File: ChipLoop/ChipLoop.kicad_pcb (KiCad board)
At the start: 2 copper layers, 100 x 60 mm, 33 parts, among them J1 Conn_02x25_Counter_Clockwise, J2 Jumper, Q1 2N3904, SW1 SW_A, SW2 SW_B, U1 ATtiny84A-PU, U2 ISD1820P, U3 L78L05_TO92

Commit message: Finalized changes to chip loop input and output
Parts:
- removed the C4 at (90.3, 85.0)
- removed the C5 at (176.2, 86.4)
- removed C6: 0.001uF, libraries:C_Flat_L7.2_H6.5
- added R1: 47K, Resistor_THT:R_Axial_DIN0207_L6.3mm_D2.5mm_P10.16mm_Horizontal, F.Cu at (169.8, 108.0)
- added R3: 47K, Resistor_THT:R_Axial_DIN0207_L6.3mm_D2.5mm_P10.16mm_Horizontal, F.Cu at (127.5, 107.7)
- added R7: 1K, Resistor_THT:R_Axial_DIN0207_L6.3mm_D2.5mm_P10.16mm_Horizontal, F.Cu at (155.2, 91.3)
- C2: value 0.1uF -> 100uF; footprint libraries:C_Flat_L7.2_H6.5 -> libraries:CP_Radial_D6.3mm_P2.50mm
- C3: value 0.1uF -> 220uF; footprint libraries:C_Flat_L7.2_H6.5 -> libraries:CP_Radial_D6.3mm_P2.50mm
- R2: value 4.7K -> 1K
- moved C3 89.5 mm to (90.3, 85.0)
- moved C2 32.9 mm to (177.7, 85.0)
- moved R2 32.4 mm to (159.6, 111.5)
- moved C1 0.17 mm to (128.4, 100.8)
- renumbered C7 to C4, C8 to C5, D2 to D1, D3 to D2, D1 to D3, J2 to J1, J1 to J2, R4 to R10, R9 to R11, R10 to R12, R6 to R4, R7 to R5, R8 to R6, R1 to R8, R5 to R9
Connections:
- C1 pad 1: GND -> Net-(C1-Pad1)
- C1 pad 2: +5V -> Net-(C1-Pad2)
- C2 pad 2: /Input -> Net-(C2-Pad2)
- R2 pad 1: Net-(C4-Pad1) -> GND
- R2 pad 2: /Input -> Net-(R1-Pad1)
- R8 pad 1: Net-(C4-Pad1) -> Net-(C3-Pad1)
- RV1 pad 1: Net-(RV1-Pad1) -> Net-(R7-Pad1)
- U2 pad 14: GND -> (no net)
- U2 pad 4: Net-(C2-Pad1) -> Net-(C1-Pad2)
- U2 pad 5: Net-(C3-Pad1) -> (no net)
- U2 pad 6: Net-(C5-Pad1) -> (no net)
- U2 pad 9: Net-(RV1-Pad1) -> Net-(C2-Pad1)
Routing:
- net Net-(C4-Pad1): track 81.3 -> 0.00 mm, vias 1 -> 0
- net Net-(RV1-Pad1): track 53.9 -> 0.00 mm, vias 1 -> 0
- net Net-(C1-Pad2): track 0.00 -> 50.0 mm, vias 0 -> 1
- net Net-(C5-Pad1): track 45.8 -> 0.00 mm
- net Net-(R1-Pad1): track 0.00 -> 36.6 mm, vias 0 -> 1
- net Net-(C2-Pad2): track 0.00 -> 33.7 mm
- net /FT: track 73.9 -> 104.0 mm
- net Net-(R7-Pad1): track 0.00 -> 26.0 mm, vias 0 -> 1
- net /Input: track 238.7 -> 225.3 mm
- net /PLAYL: track 82.5 -> 71.5 mm, vias 1 -> 2
- net +5V: track 182.9 -> 172.1 mm
- net Net-(C3-Pad1): track 22.2 -> 12.0 mm
- net Net-(C2-Pad1): track 13.9 -> 23.3 mm
- net /REC: track 71.0 -> 62.3 mm
- net GND: track 41.6 -> 50.3 mm, vias 21 -> 6
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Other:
- board text added: "Chip Loop V1.1"
- board text removed: "Chip Loop V1.0"

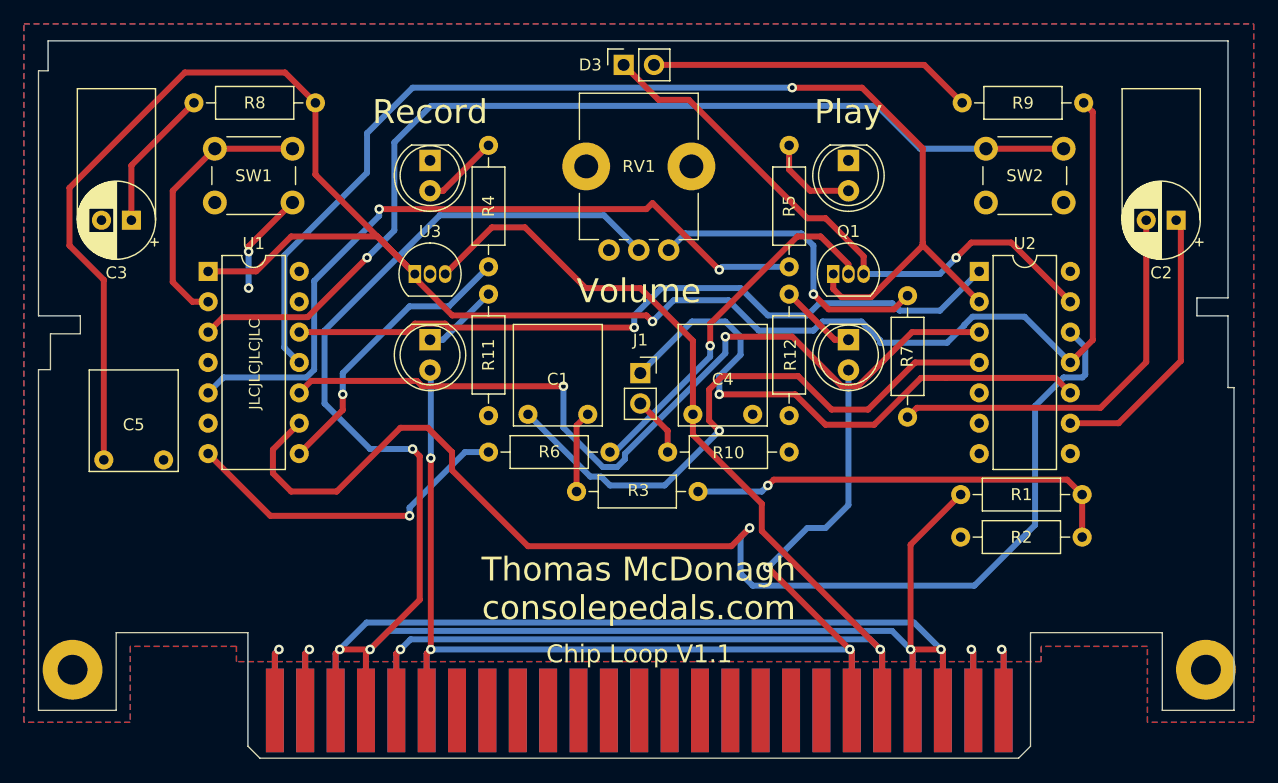
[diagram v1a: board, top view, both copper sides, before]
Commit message: Finalized new version of ChipLoop board
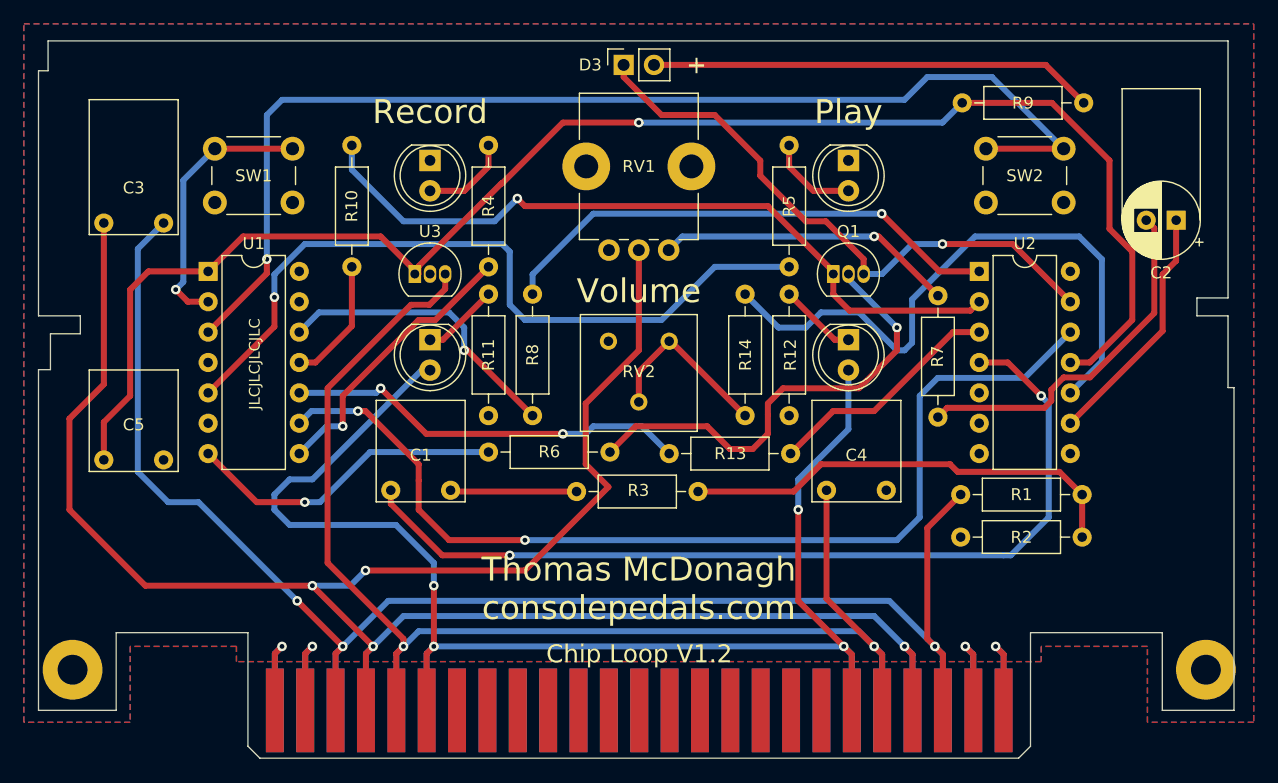
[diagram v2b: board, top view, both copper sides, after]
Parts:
- removed J1: Jumper, Connector_PinSocket_2.54mm:PinSocket_1x02_P2.54mm_Vertical
- added R13: 47K, Resistor_THT:R_Axial_DIN0207_L6.3mm_D2.5mm_P10.16mm_Horizontal, F.Cu at (145.4, 104.5)
- added R14: 82K, Resistor_THT:R_Axial_DIN0207_L6.3mm_D2.5mm_P10.16mm_Horizontal, F.Cu at (141.6, 101.3)
- added RV2: 100K, Potentiometer_THT:Potentiometer_Bourns_3386F_Vertical, F.Cu at (130.2, 95.1)
- C3: value 220uF -> 1uF; footprint libraries:CP_Radial_D6.3mm_P2.50mm -> libraries:C_Flat_L7.2_H10
- R10: value 100K -> 47K
- R8: value 1K -> 47K
- moved R10 36.8 mm to (108.7, 78.7), turned to 270 degrees
- moved R8 32.5 mm to (123.8, 91.2), turned to 270 degrees
- moved C1 13.1 mm to (117.0, 107.2)
- moved C4 12.9 mm to (153.4, 107.2)
- moved C3 2.70 mm to (93.0, 84.8)
- moved R7 2.54 mm to (157.7, 91.3)
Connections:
- C3 pad 1: Net-(C3-Pad1) -> /Input
- C3 pad 2: GND -> /Output
- J2 pad 22: /Input -> /Output
- J2 pad 29: /Input -> /Output
- J2 pad 4: /Input -> /Output
- J2 pad 47: /Input -> /Output
- Q1 pad 1: /PLAYE -> Net-(Q1-Pad1)
- R10 pad 1: Net-(J1-Pad2) -> Net-(Q1-Pad1)
- R10 pad 2: GND -> /PLAYE
- R8 pad 1: Net-(C3-Pad1) -> Net-(R8-Pad1)
- R8 pad 2: +5V -> /REC
- R9 pad 1: Net-(D3-Pad2) -> +5V
- R9 pad 2: +5V -> Net-(D3-Pad2)
- RV1 pad 2: /Input -> /Output
- U2 pad 1: /REC -> Net-(R8-Pad1)
- U2 pad 2: /PLAYE -> Net-(Q1-Pad1)
- U2 pad 3: /PLAYL -> Net-(R13-Pad1)
- U2 pad 7: GND -> (no net)
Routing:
- net /Output: track 0.00 -> 174.9 mm, vias 0 -> 4
- net /Input: track 225.3 -> 134.2 mm, vias 5 -> 3
- net /PLAYE: track 98.6 -> 10.6 mm, vias 1 -> 0
- net Net-(Q1-Pad1): track 0.00 -> 62.4 mm, vias 0 -> 1
- net Net-(R8-Pad1): track 0.00 -> 43.1 mm, vias 0 -> 1
- net +5V: track 172.1 -> 129.4 mm
- net /PLAYL: track 71.5 -> 33.9 mm
- net /REC: track 62.3 -> 24.9 mm
- net Net-(C1-Pad2): track 50.0 -> 76.0 mm, vias 1 -> 2
- net Net-(R13-Pad1): track 0.00 -> 20.0 mm
- net /FT: track 104.0 -> 84.8 mm, vias 1 -> 2
- net Net-(R14-Pad1): track 0.00 -> 15.1 mm
- net /LEDPower: track 109.1 -> 123.9 mm
- net Net-(C3-Pad1): track 12.0 -> 0.00 mm
- net /SW_B: track 85.2 -> 97.1 mm
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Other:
- board text added: "+"
- board text added: "Chip Loop V1.2"
- board text removed: "Chip Loop V1.1"
